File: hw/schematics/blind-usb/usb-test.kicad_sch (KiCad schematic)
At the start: 33 parts, among them Q1 MMBT3906LT1G, U1 TPS259470LRPWR, U2 STUSB4500QTR

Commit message: Correct USB connector lands and document PD factory policy evidence
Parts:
- USBC1: footprint UNKNOWN_TYPE_C_31_M_12:USB-C_SMD-TYPE-C-31-M-12_1 -> blind-usb:HRO_TYPE_C_31_M_12
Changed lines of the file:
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@@
     (property
       "Footprint"
-      "UNKNOWN_TYPE_C_31_M_12:USB-C_SMD-TYPE-C-31-M-12_1"
+      "blind-usb:HRO_TYPE_C_31_M_12"
       (at 48.26 74.93 0)
       (effects

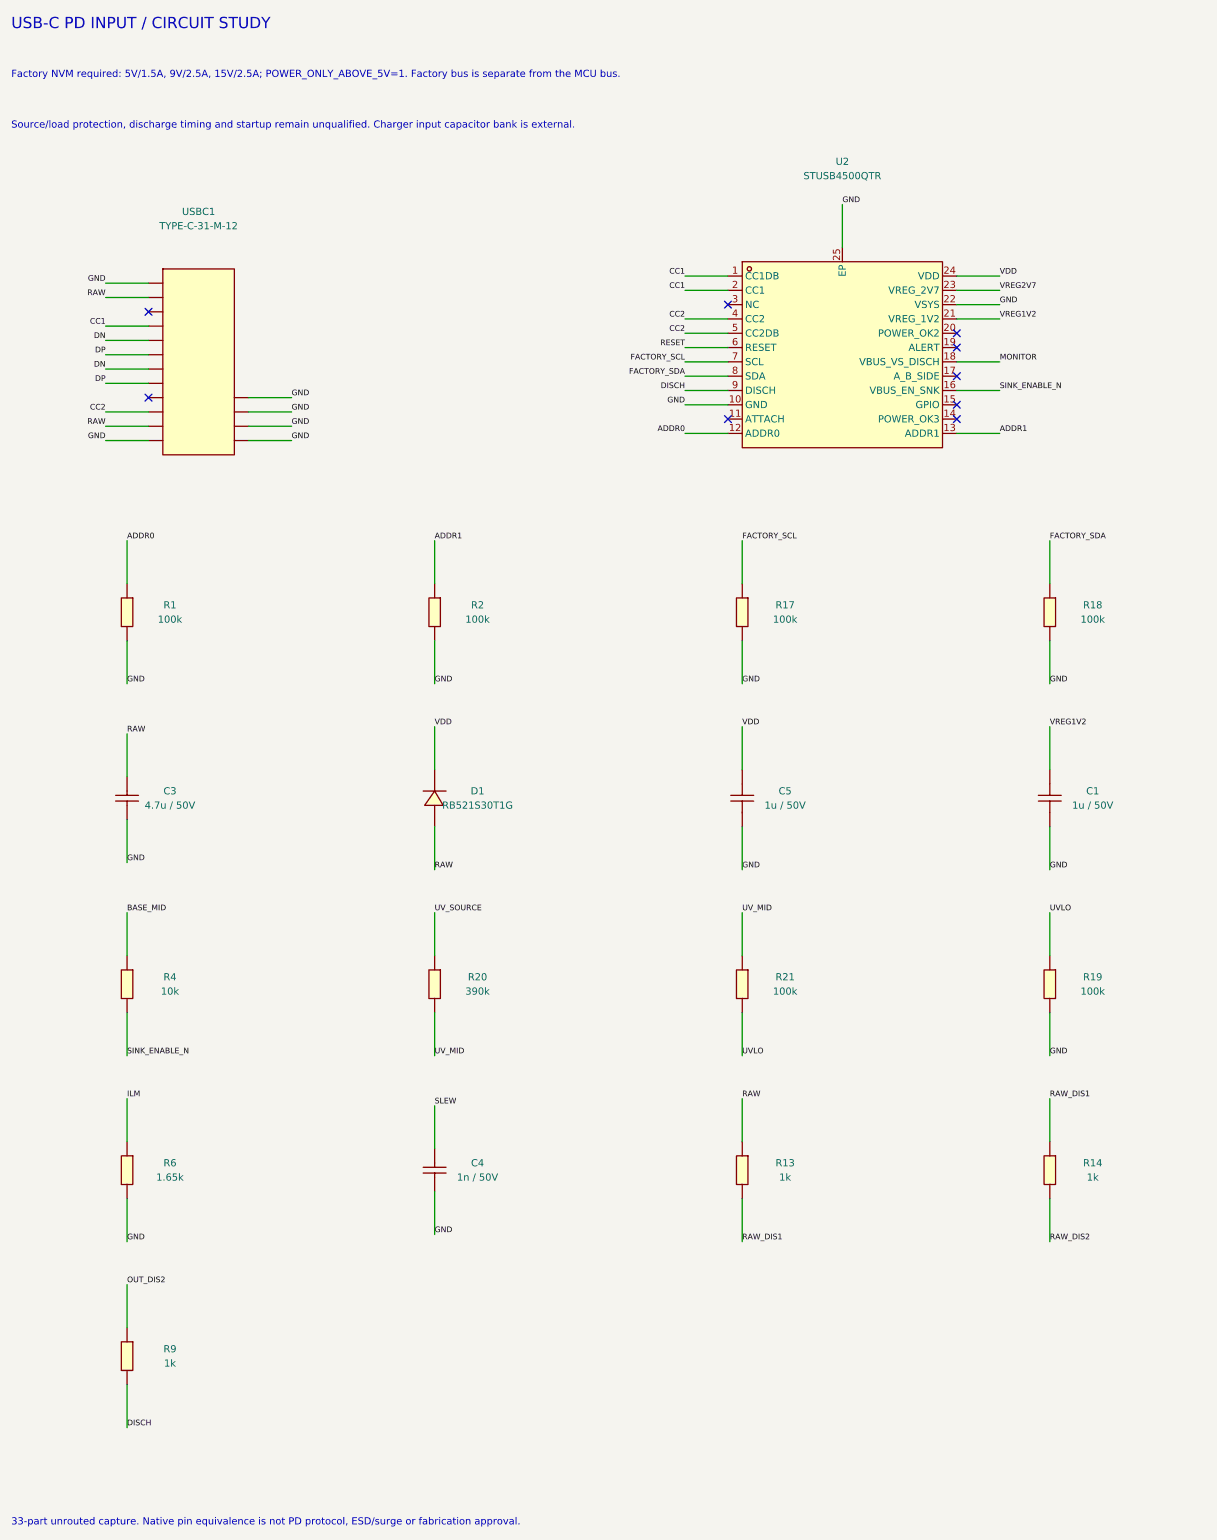
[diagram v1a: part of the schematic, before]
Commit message: Wire monitored USB power into the circuit and owned sensor runtime
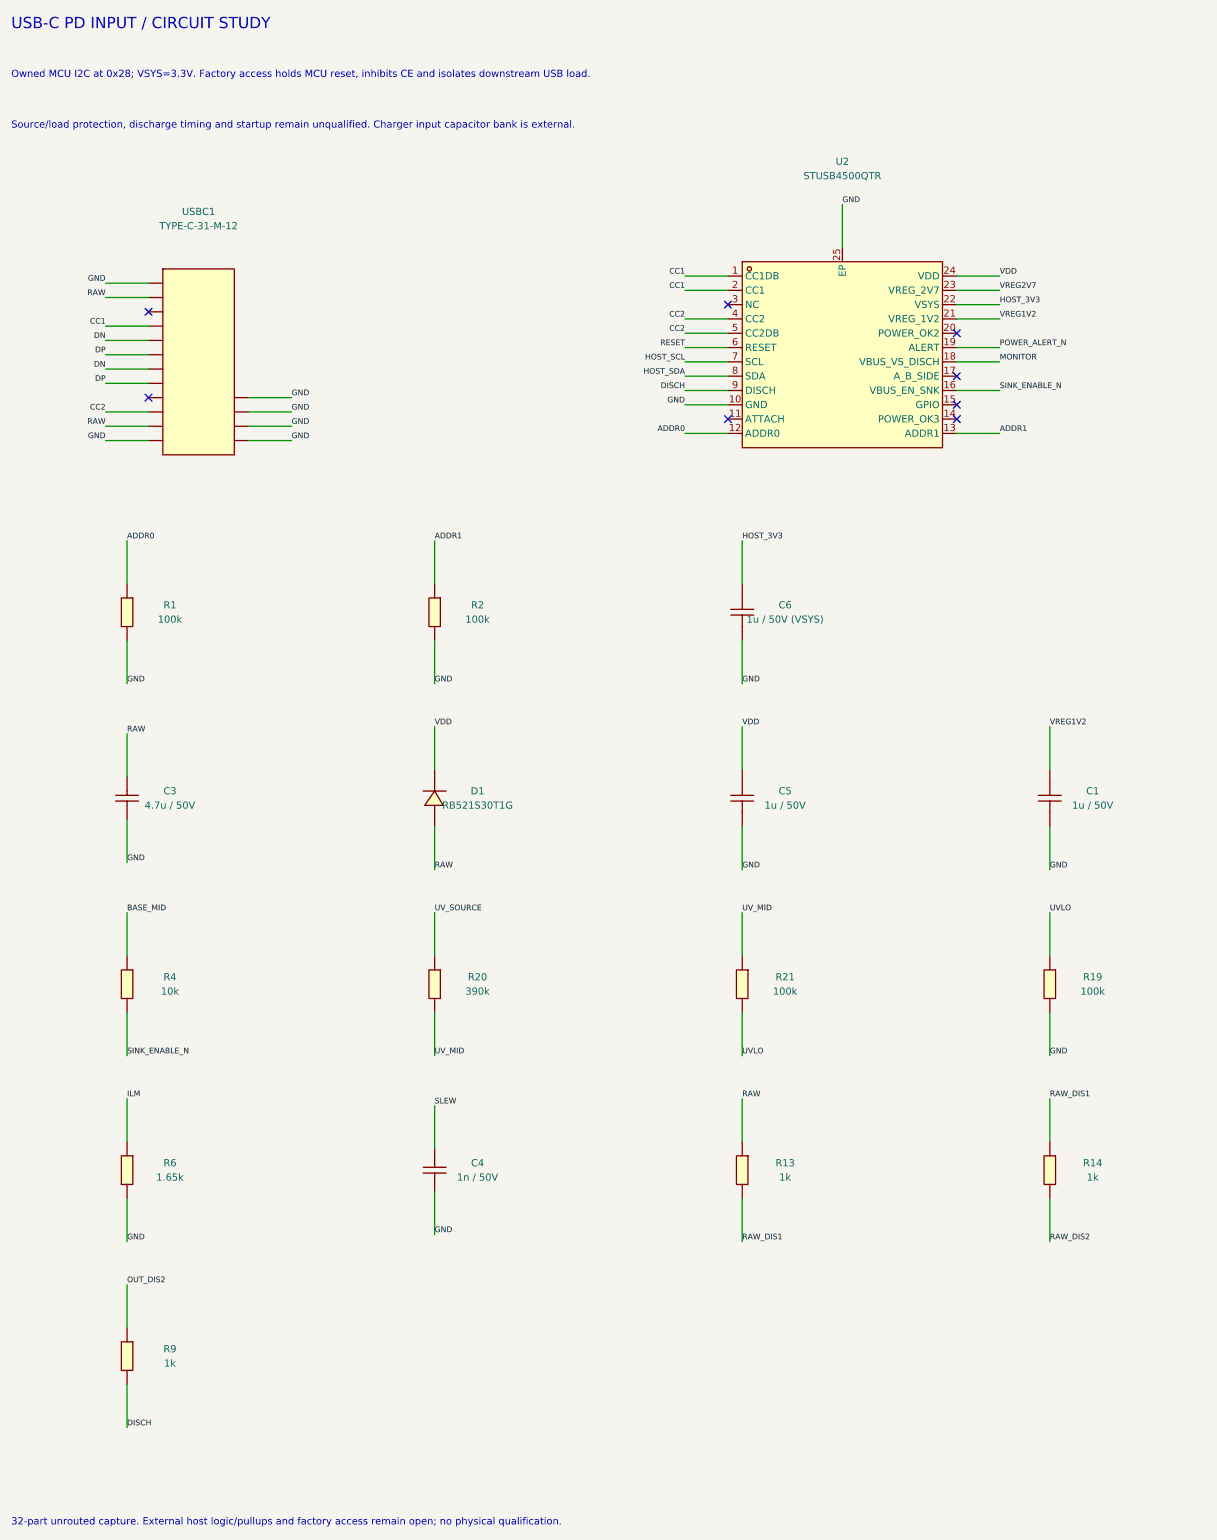
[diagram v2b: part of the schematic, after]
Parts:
- removed R17, R18: 100k, blind-control-io:R0402, symbol SmartBlinds:P_0402WGF1003TCE
- added C6: 1u / 50V (VSYS), SAMSUNG_CL10A105KB8NNNC:C0603, symbol SmartBlinds:P_CL10A105KB8NNNC
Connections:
- net GND: now also C6.2; no longer U2.22 (VSYS)
- net POWER_ALERT_N: now reaches U2.19 (ALERT)
- net FACTORY_SCL renamed HOST_SCL
- net FACTORY_SDA renamed HOST_SDA
- new net HOST_3V3: C6.1, U2.22 (VSYS)
- no-connect marks 12 -> 11
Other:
- note added: "32-part unrouted capture. External host logic/pullups and factory access remain open; no physical qualification."
- note added: "Owned MCU I2C at 0x28; VSYS=3.3V. Factory access holds MCU reset, inhibits CE and isolates downstream USB load."
- note removed: "33-part unrouted capture. Native pin equivalence is not PD protocol, ESD/surge or fabrication approval."
- note removed: "Factory NVM required: 5V/1.5A, 9V/2.5A, 15V/2.5A; POWER_ONLY_ABOVE_5V=1. Factory bus is separate from the MCU bus."
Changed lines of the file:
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@@
   (wire
     (pts
+      (xy 144.78 124.46)
+      (xy 144.78 132.08))
+    (stroke
+      (width 0)
+      (type default))
+)
+  (label
+    "GND"
+    (at 144.78 132.08 0)
+    (effects
+      (font
+        (size 1.0 1.0))
+      (justify left bottom))
+)
+  (wire
+    (pts
+      (xy 144.78 114.3)
+      (xy 144.78 106.68))
+    (stroke
+      (width 0)
+      (type default))
+)
+  (label
+    "HOST_3V3"
+    (at 144.78 106.68 0)
+    (effects
+      (font
+        (size 1.0 1.0))
+      (justify left bottom))
+)
+  (symbol
+    (lib_id "SmartBlinds:P_CL10A105KB8NNNC")
+    (at 144.78 119.38 270)
+    (unit 1)
+    (in_bom yes)
+    (on_board yes)
+    (dnp no)
+    (property
+      "Reference"
+      "C6"
+      (at 152.4 118.11 270)
+      (effects
+        (font
+          (size 1.27 1.27))))
+    (property
+      "Value"
+      "1u / 50V (VSYS)"
+      (at 152.4 120.65 270)
+      (effects
+        (font
+          (size 1.27 1.27))))
+    (property
+      "Footprint"
+      "SAMSUNG_CL10A105KB8NNNC:C0603"
+      (at 144.78 119.38 0)
+      (effects
+        (font
+          (size 1.27 1.27))
+        (hide yes)))
+    (property
+      "MPN"
+      "CL10A105KB8NNNC"
+      (at 144.78 119.38 0)
+      (effects
+        (font
+          (size 1.27 1.27))
+        (hide yes)))
+    (property
+      "LCSC"
+      "C15849"
+      (at 144.78 119.38 0)
+      (effects
+        (font
+          (size 1.27 1.27))
+        (hide yes)))
+    (property
+      "atopile_address"
+      "usb.c_vsys"
+      (at 144.78 119.38 0)
+      (effects
+        (font
+          (size 1.27 1.27))
+        (hide yes)))
+    (instances
+      (project
+        "usb-test"
+        (path
+          "/55aff08a-e9ee-5259-a283-dc8e6e73fd3a"
+          (reference "C6")
+          (unit 1))))
+    (pin
+      "2"
+)
+    (pin
+      "1"
+))
+  (wire
+    (pts
       (xy 90.17 157.48)
       (xy 90.17 165.1))
@@
   (wire
     (pts
-      (xy 144.78 124.46)
-      (xy 144.78 132.08))
-    (stroke
-      (width 0)
-      (type default))
-)
-  (label
-    "GND"
-    (at 144.78 132.08 0)
-    (effects
-      (font
-        (size 1.0 1.0))
-      (justify left bottom))
-)
-  (wire
-    (pts
-      (xy 144.78 114.3)
-      (xy 144.78 106.68))
-    (stroke
-      (width 0)
-      (type default))
-)
-  (label
-    "FACTORY_SCL"
-    (at 144.78 106.68 0)
-    (effects
-      (font
-        (size 1.0 1.0))
-      (justify left bottom))
-)
-  (symbol
-    (lib_id "SmartBlinds:P_0402WGF1003TCE")
-    (at 144.78 119.38 270)
-    (unit 1)
-    (in_bom yes)
-    (on_board yes)
-    (dnp no)
-    (property
-      "Reference"
-      "R17"
-      (at 152.4 118.11 270)
-      (effects
-        (font
-          (size 1.27 1.27))))
-    (property
-      "Value"
-      "100k"
-      (at 152.4 120.65 270)
-      (effects
-        (font
-          (size 1.27 1.27))))
-    (property
-      "Footprint"
-      "blind-control-io:R0402"
-      (at 144.78 119.38 0)
-      (effects
-        (font
-          (size 1.27 1.27))
-        (hide yes)))
-    (property
-      "MPN"
-      "0402WGF1003TCE"
-      (at 144.78 119.38 0)
-      (effects
-        (font
-          (size 1.27 1.27))
-        (hide yes)))
-    (property
-      "LCSC"
-      "C25741"
-      (at 144.78 119.38 0)
-      (effects
-        (font
-          (size 1.27 1.27))
-        (hide yes)))
-    (property
-      "atopile_address"
-      "usb.r_scl"
-      (at 144.78 119.38 0)
-      (effects
-        (font
-          (size 1.27 1.27))
-        (hide yes)))
-    (instances
-      (project
-        "usb-test"
-        (path
-          "/55aff08a-e9ee-5259-a283-dc8e6e73fd3a"
-          (reference "R17")
-          (unit 1))))
-    (pin
-      "2"
-)
-    (pin
-      "1"
-))
-  (wire
-    (pts
-      (xy 199.39 124.46)
-      (xy 199.39 132.08))
-    (stroke
-      (width 0)
-      (type default))
-)
-  (label
-    "GND"
-    (at 199.39 132.08 0)
-    (effects
-      (font
-        (size 1.0 1.0))
-      (justify left bottom))
-)
-  (wire
-    (pts
-      (xy 199.39 114.3)
-      (xy 199.39 106.68))
-    (stroke
-      (width 0)
-      (type default))
-)
-  (label
-    "FACTORY_SDA"
-    (at 199.39 106.68 0)
-    (effects
-      (font
-        (size 1.0 1.0))
-      (justify left bottom))
-)
-  (symbol
-    (lib_id "SmartBlinds:P_0402WGF1003TCE")
-    (at 199.39 119.38 270)
-    (unit 1)
-    (in_bom yes)
-    (on_board yes)
-    (dnp no)
-    (property
-      "Reference"
-      "R18"
-      (at 207.01 118.11 270)
-      (effects
-        (font
-          (size 1.27 1.27))))
-    (property
-      "Value"
-      "100k"
-      (at 207.01 120.65 270)
-      (effects
-        (font
-          (size 1.27 1.27))))
-    (property
-      "Footprint"
-      "blind-control-io:R0402"
-      (at 199.39 119.38 0)
-      (effects
-        (font
-          (size 1.27 1.27))
-        (hide yes)))
-    (property
-      "MPN"
-      "0402WGF1003TCE"
-      (at 199.39 119.38 0)
-      (effects
-        (font
-          (size 1.27 1.27))
-        (hide yes)))
-    (property
-      "LCSC"
-      "C25741"
-      (at 199.39 119.38 0)
-      (effects
-        (font
-          (size 1.27 1.27))
-        (hide yes)))
-    (property
-      "atopile_address"
-      "usb.r_sda"
-      (at 199.39 119.38 0)
-      (effects
-        (font
-          (size 1.27 1.27))
-        (hide yes)))
-    (instances
-      (project
-        "usb-test"
-        (path
-          "/55aff08a-e9ee-5259-a283-dc8e6e73fd3a"
-          (reference "R18")
-          (unit 1))))
-    (pin
-      "2"
-)
-    (pin
-      "1"
-))
-  (wire
-    (pts
       (xy 199.39 190.5)
       (xy 199.39 198.12))
@@
 )
   (label
-    "FACTORY_SCL"
+    "HOST_SCL"
     (at 134.62 74.93 0)
     (effects
@@
 )
   (label
-    "FACTORY_SDA"
+    "HOST_SDA"
     (at 134.62 77.47 0)
     (effects
@@
       (justify left bottom))
 )
-  (no_connect
-    (at 182.88 72.39)
+  (wire
+    (pts
+      (xy 182.88 72.39)
+      (xy 190.5 72.39))
+    (stroke
+      (width 0)
+      (type default))
+)
+  (label
+    "POWER_ALERT_N"
+    (at 190.5 72.39 0)
+    (effects
+      (font
+        (size 1.0 1.0))
+      (justify left bottom))
 )
   (no_connect
@@
 )
   (label
-    "GND"
+    "HOST_3V3"
     (at 190.5 64.77 0)
     (effects
@@
 )
   (text
-    "Factory NVM required: 5V/1.5A, 9V/2.5A, 15V/2.5A; POWER_ONLY_ABOVE_5V=1. Factory bus is separate from the MCU bus."
+    "Owned MCU I2C at 0x28; VSYS=3.3V. Factory access holds MCU reset, inhibits CE and isolates downstream USB load."
     (at 15 24 0)
     (effects
@@
 )
   (text
-    "33-part unrouted capture. Native pin equivalence is not PD protocol, ESD/surge or fabrication approval."
+    "32-part unrouted capture. External host logic/pullups and factory access remain open; no physical qualification."
     (at 15 281 0)
     (effects

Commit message: Make the cleaner controller reproducible from circuit source (#3)
* Rebuild cleaner controller from circuit source and verify native previews

* Use compiler-compatible Python without changing native render runtime
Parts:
- added C7: 47n / 50V, blind-power:C0402, symbol SmartBlinds:P_0402B473K500NT
- added C8: 4.7u / 50V, blind-usb:C1206, symbol SmartBlinds:P_CL31A475KBHNNNE
- added R17: 1.2k, blind-core:R0402, symbol SmartBlinds:P_0402WGF1201TCE
- added R18: 402k, blind-usb-protection:R0402, symbol SmartBlinds:P_0402WGF4023TCE
- added R22: 30.1k / 0.1%, blind-usb-protection:R0402, symbol SmartBlinds:P_RT0402BRD0730K1L
- added R23: 390k, UNI_ROYAL_0402WGF3903TCE:R0402, symbol SmartBlinds:P_0402WGF3903TCE
- added R24: 100k, blind-control-io:R0402, symbol SmartBlinds:P_0402WGF1003TCE
- added R25: 4.7k, blind-control-io:R0402, symbol SmartBlinds:P_0402WGF4701TCE
- added U3: TPS26600PWPR, blind-usb-protection:TPS26600_PWP16, symbol SmartBlinds:P_TPS26600PWPR
- added U4: TVS1800DRVR, blind-usb-protection:TVS1800_DRV6, symbol SmartBlinds:P_TVS1800DRVR
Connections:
- net GND: now also C8.2, R24.2, U3.9 (GND), U4.1 (GND), U4.2 (GND), U4.3 (GND), U4.7 (GND)
- net RAW: now also R23.1, U3.1 (IN), U3.2 (IN), U3.3 (UVLO); no longer D1.2 (A), Q1.2 (E), R11.1, R13.1, R5.1, U1.5 (IN)
- new net CUT_ILIM: R17.1, U3.11 (ILIM)
- new net CUT_ILIM_MID: R17.2, R25.1
- new net CUT_MODE: R18.1, U3.6 (MODE)
- new net CUT_OVP: R22.1, R23.2, U3.5 (OVP)
- new net CUT_RTN: C7.2, R18.2, R22.2, R25.2, U3.17 (EP), U3.8 (RTN)
- new net CUT_SLEW: C7.1, U3.12 (dVdT)
- new net GUARDED: C8.1, D1.2 (A), Q1.2 (E), R11.1, R13.1, R24.1, R5.1, U1.5 (IN), U3.15 (OUT), U3.16 (OUT), U4.4 (IN), U4.5 (IN), U4.6 (IN)
- no-connect marks 11 -> 16
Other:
- note added: "42-part UNVERIFIED capture. Thermal stitching, IC placement, routing, fixture and physical tests remain open."
- note added: "Raw cutoff + guarded PD + contract-gated charger. 21 V cutoff response and pulse coordination require measurement."
- note removed: "32-part unrouted capture. External host logic/pullups and factory access remain open; no physical qualification."
- note removed: "Source/load protection, discharge timing and startup remain unqualified. Charger input capacitor bank is external."
